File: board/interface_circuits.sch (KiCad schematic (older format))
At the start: 44 parts, among them J1 Conn_01x03, J2 Conn_01x04, Q1 MMBT3904, Q2 MMBT3904, Q3 MMBT3904, Q4 MMBT3904, U1 TPS77633_SO8, U2 STMPS2151_SOT23-5

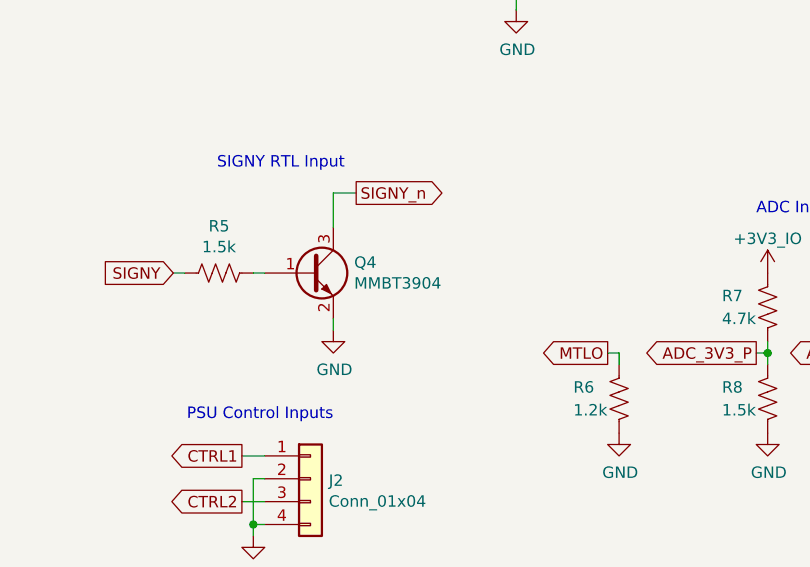
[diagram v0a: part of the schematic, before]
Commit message: Board: changed the SIGNY transistor to MMBT2369 since the 3904 has slow saturation recovery
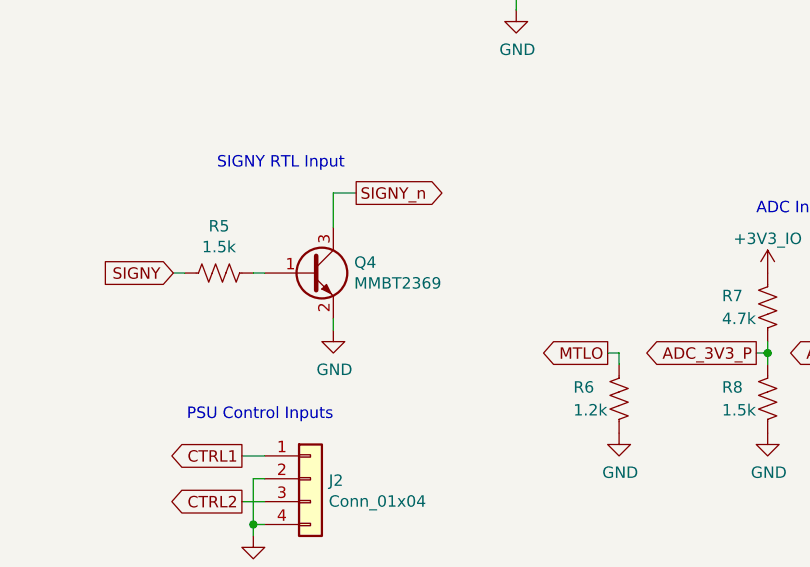
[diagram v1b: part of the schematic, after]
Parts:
- removed Q4: MMBT3904, Package_TO_SOT_SMD:SOT-23, symbol Transistor_BJT:MMBT3904
- added Q4: MMBT2369, Package_TO_SOT_SMD:SOT-23, symbol agc_monitor:MMBT2369
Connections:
- net GND: now also Q4.2 (E)
- net SIGNY_n: now also Q4.3 (C)
- net at R5.1: now also Q4.1 (B)
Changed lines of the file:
@@
-$EndComp
-$Comp
-L Transistor_BJT:MMBT3904 Q4
-U 1 1 5C96DCC2
-P 2000 5550
-F 0 "Q4" H 2191 5596 50  0000 L CNN
-F 1 "MMBT3904" H 2191 5505 50  0000 L CNN
-F 2 "Package_TO_SOT_SMD:SOT-23" H 2200 5475 50  0001 L CIN
-F 3 "https://www.fairchildsemi.com/datasheets/2N/2N3904.pdf" H 2000 5550 50  0001 L CNN
-	1    2000 5550
-	1    0    0    -1
 $EndComp
 $Comp
@@
 Wire Wire Line
 	1750 6450 1800 6450
+$Comp
+L agc_monitor:MMBT2369 Q4
+U 1 1 5CA10390
+P 2000 5550
+F 0 "Q4" H 2191 5596 50  0000 L CNN
+F 1 "MMBT2369" H 2191 5505 50  0000 L CNN
+F 2 "Package_TO_SOT_SMD:SOT-23" H 2200 5475 50  0001 L CIN
+F 3 "http://www.fairchildsemi.com/ds/BC/BC817.pdf" H 2000 5550 50  0001 L CNN
+	1    2000 5550
+	1    0    0    -1
+$EndComp
 $EndSCHEMATC

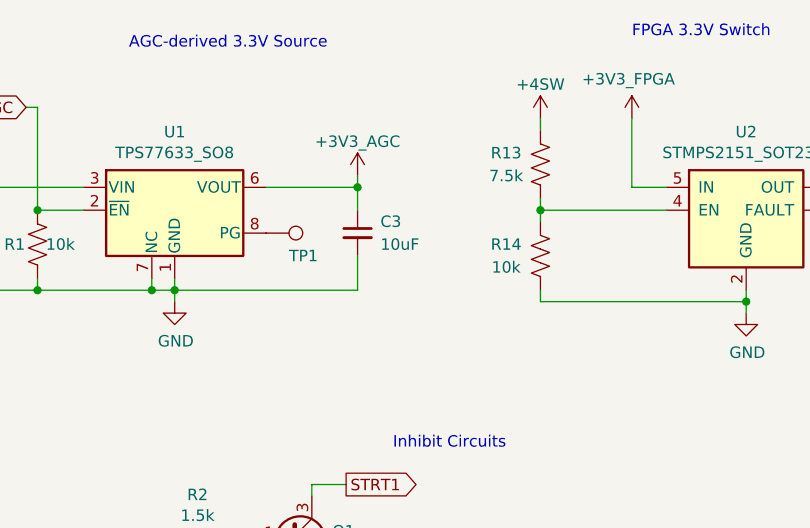
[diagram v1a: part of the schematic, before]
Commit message: Board: increased LDO output capacitor to 22uF to improve stability
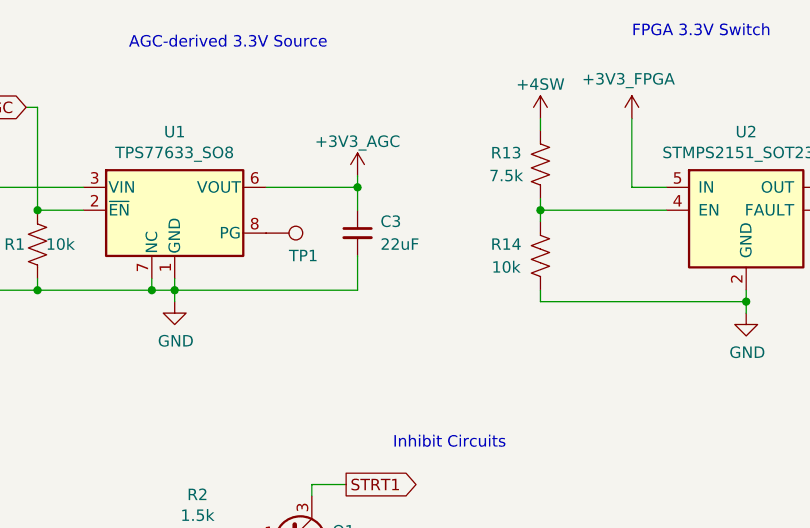
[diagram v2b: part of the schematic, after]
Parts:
- C3: value 10uF -> 22uF
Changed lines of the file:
@@
 P 3100 1950
 F 0 "C3" H 3200 2000 50  0000 L CNN
-F 1 "10uF" H 3200 1900 50  0000 L CNN
+F 1 "22uF" H 3200 1900 50  0000 L CNN
 F 2 "Capacitor_SMD:C_1206_3216Metric" H 3100 1950 50  0001 C CNN
 F 3 "~" H 3100 1950 50  0001 C CNN

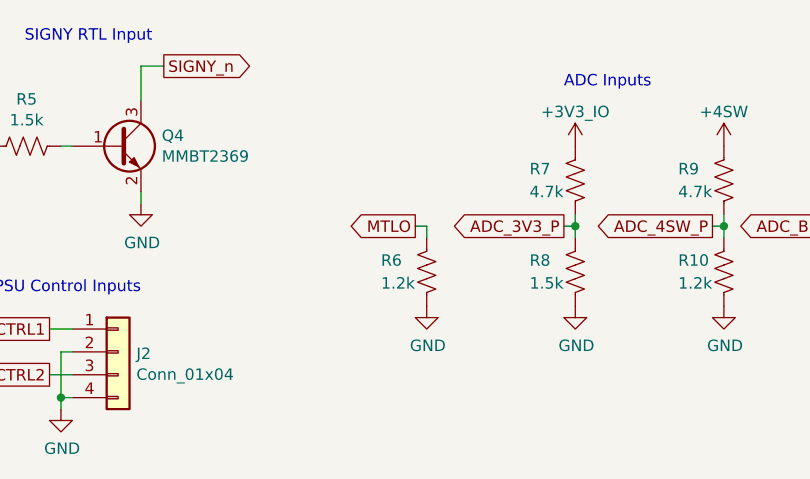
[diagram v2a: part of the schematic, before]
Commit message: Board: increased AGC temperature sense resistor to 1.5k to increase ADC sensitivity
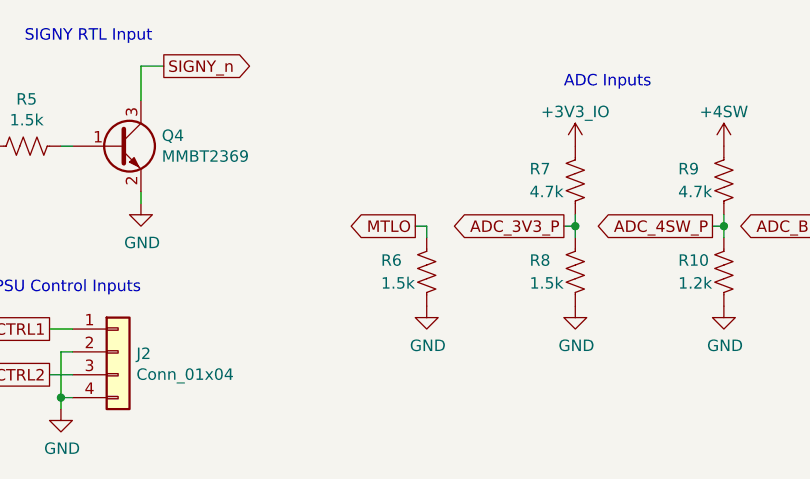
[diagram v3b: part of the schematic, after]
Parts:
- R6: value 1.2k -> 1.5k
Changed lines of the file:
@@
 EESchema Schematic File Version 4
 LIBS:agc_monitor-cache
-EELAYER 26 0
+EELAYER 29 0
 EELAYER END
 $Descr A4 11693 8268
@@
 P 3350 6100
 F 0 "R6" H 3550 6150 50  0000 R CNN
-F 1 "1.2k" H 3550 6050 50  0000 R CNN
+F 1 "1.5k" H 3550 6050 50  0000 R CNN
 F 2 "Resistor_SMD:R_0603_1608Metric" V 3390 6090 50  0001 C CNN
 F 3 "~" H 3350 6100 50  0001 C CNN
